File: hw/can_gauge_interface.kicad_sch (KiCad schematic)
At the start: 15 parts, among them J3 Power debug, J4 Power debug, J5 SPI debug, J6 I^{2}C debug, J7 CAN debug, U6 ATA6563-GAQW1

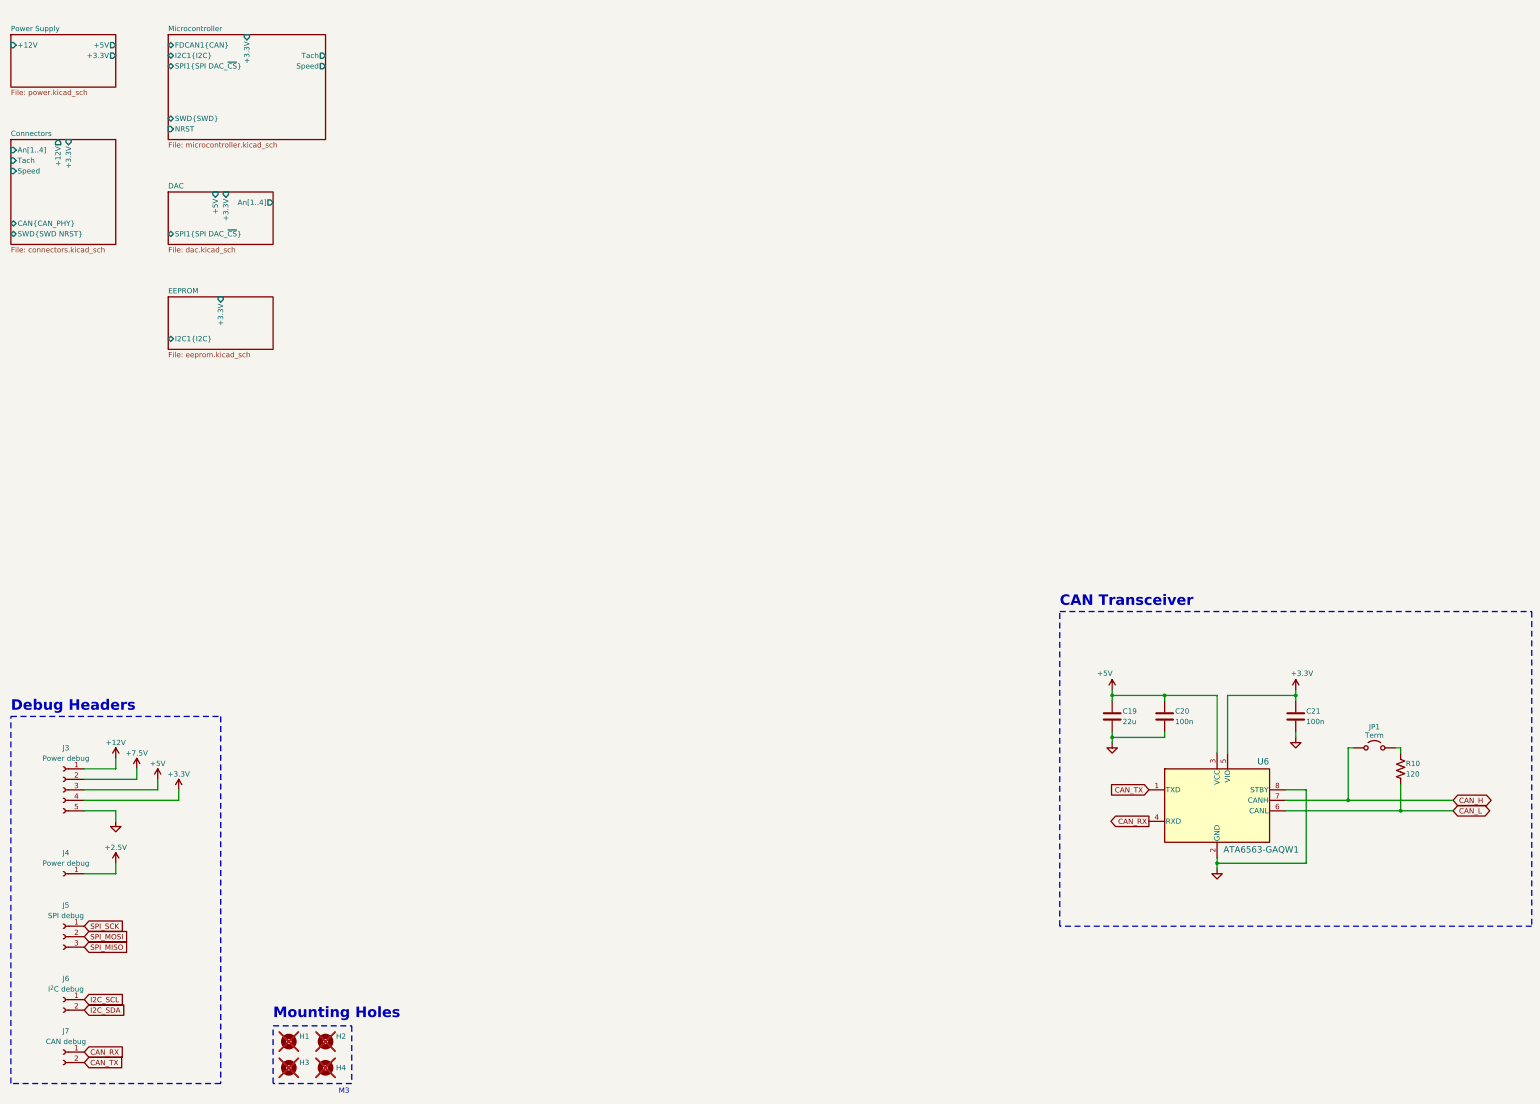
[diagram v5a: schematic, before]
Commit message: hw: can transceiver hierarchical sheet
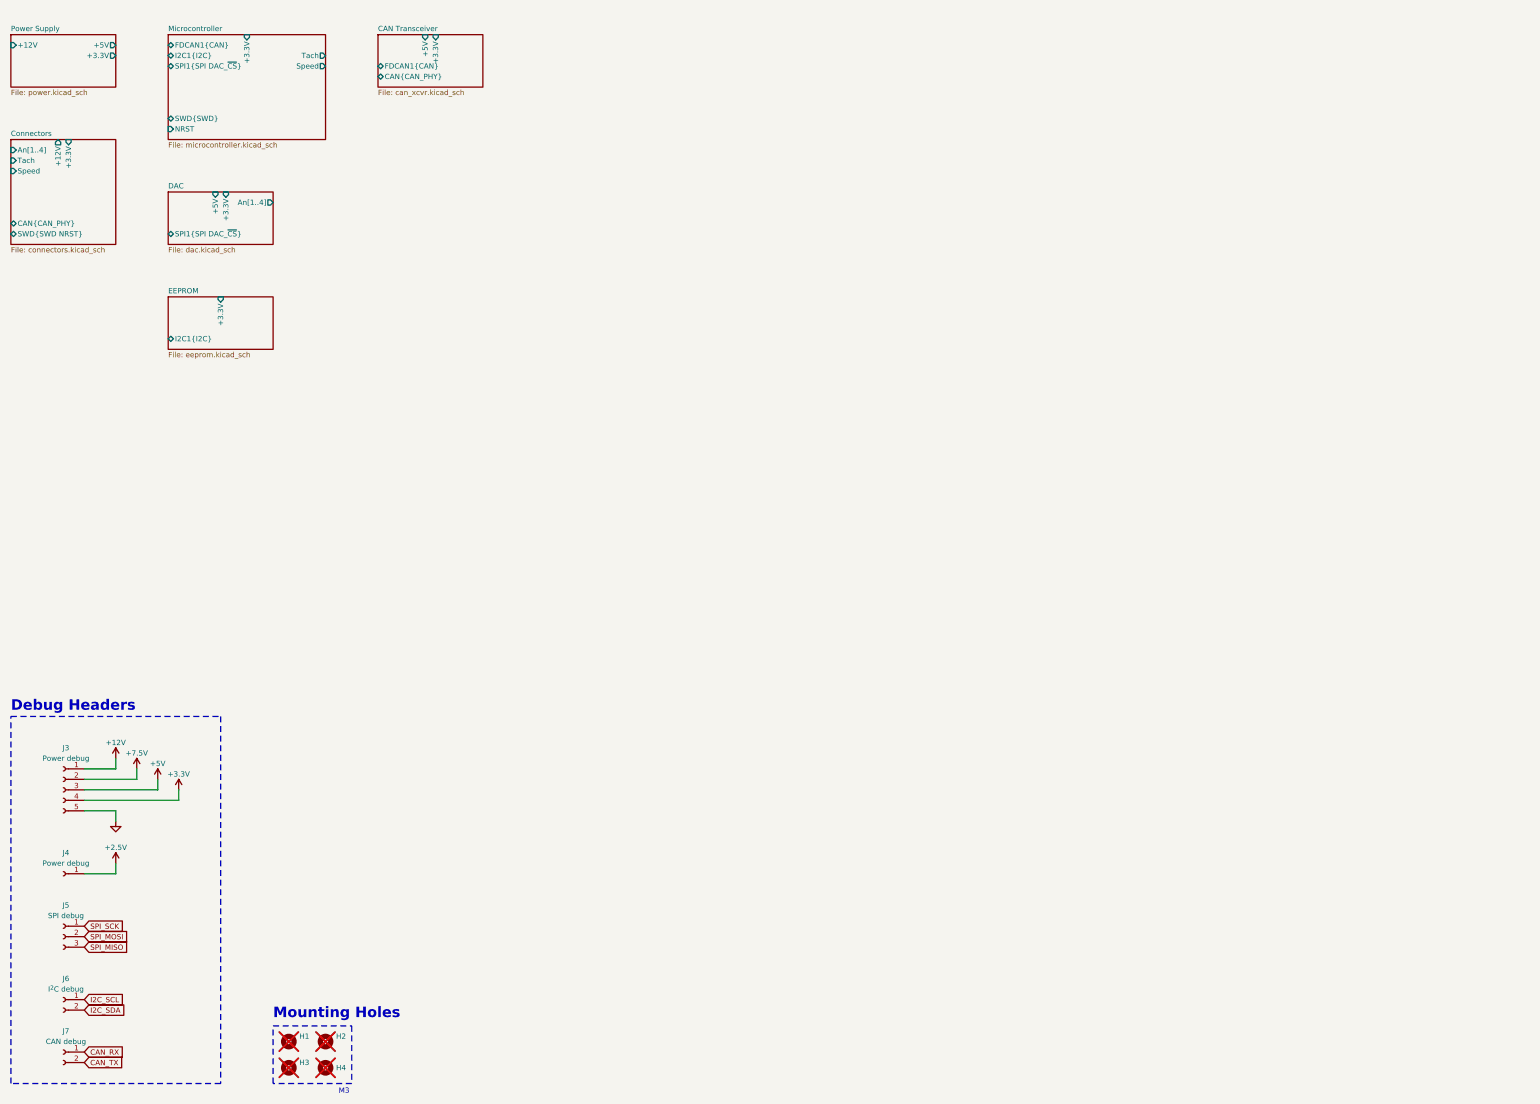
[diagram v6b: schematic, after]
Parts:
- removed C19: 22u, Capacitor_SMD:C_1206_3216Metric, symbol Device:C
- removed C20, C21: 100n, Capacitor_SMD:C_0402_1005Metric, symbol Device:C
- removed JP1: Term, TestPoint:TestPoint_2Pads_Pitch2.54mm_Drill0.8mm, symbol Jumper:Jumper_2_Open
- removed R10: 120, Resistor_SMD:R_0603_1608Metric, symbol Device:R_US
- removed U6: ATA6563-GAQW1, footprints:SOIC8_SN_MCH, symbol ATA6563-GAQW1:ATA6563-GAQW1
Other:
- added sheet CAN Transceiver (can_xcvr.kicad_sch)
- note removed: "CAN Transceiver"

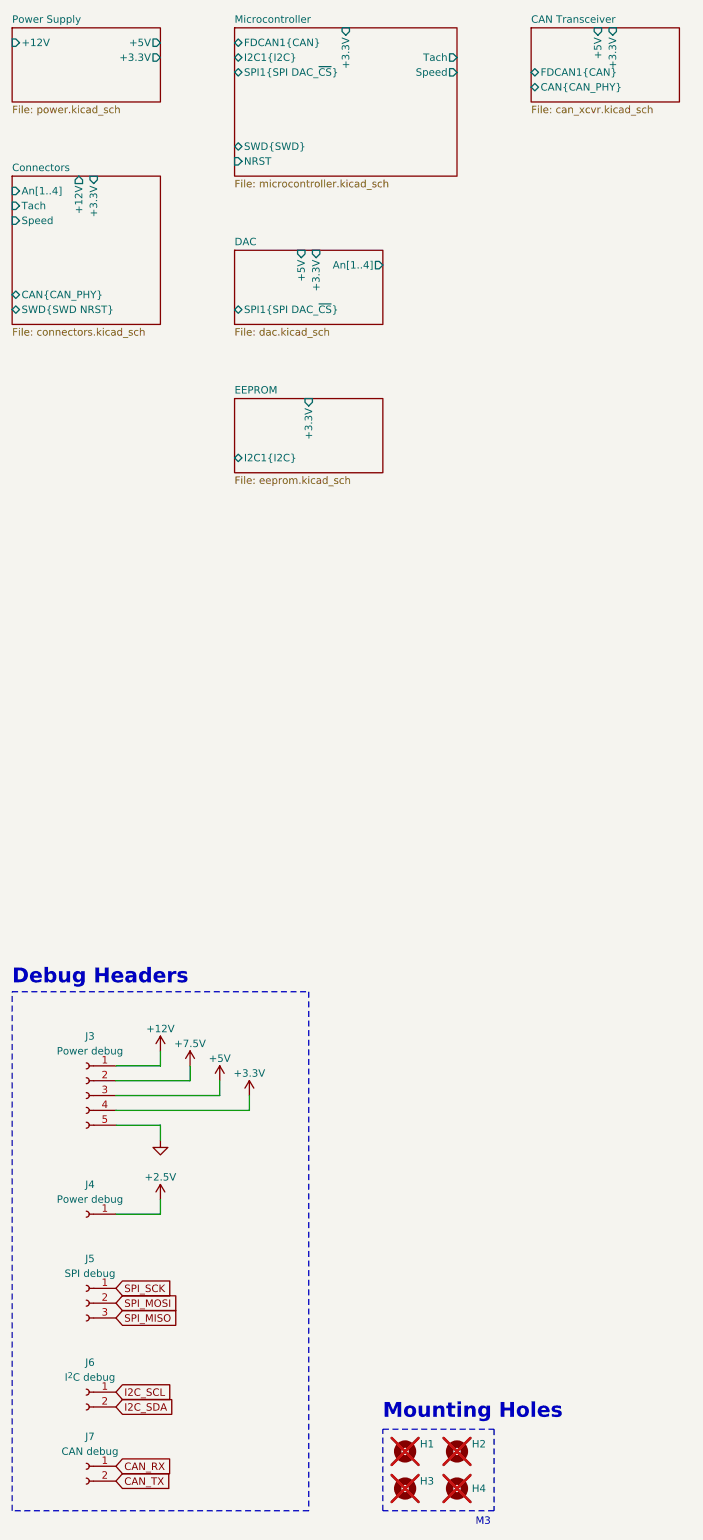
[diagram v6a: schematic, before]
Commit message: hw: headers hierarchical sheet
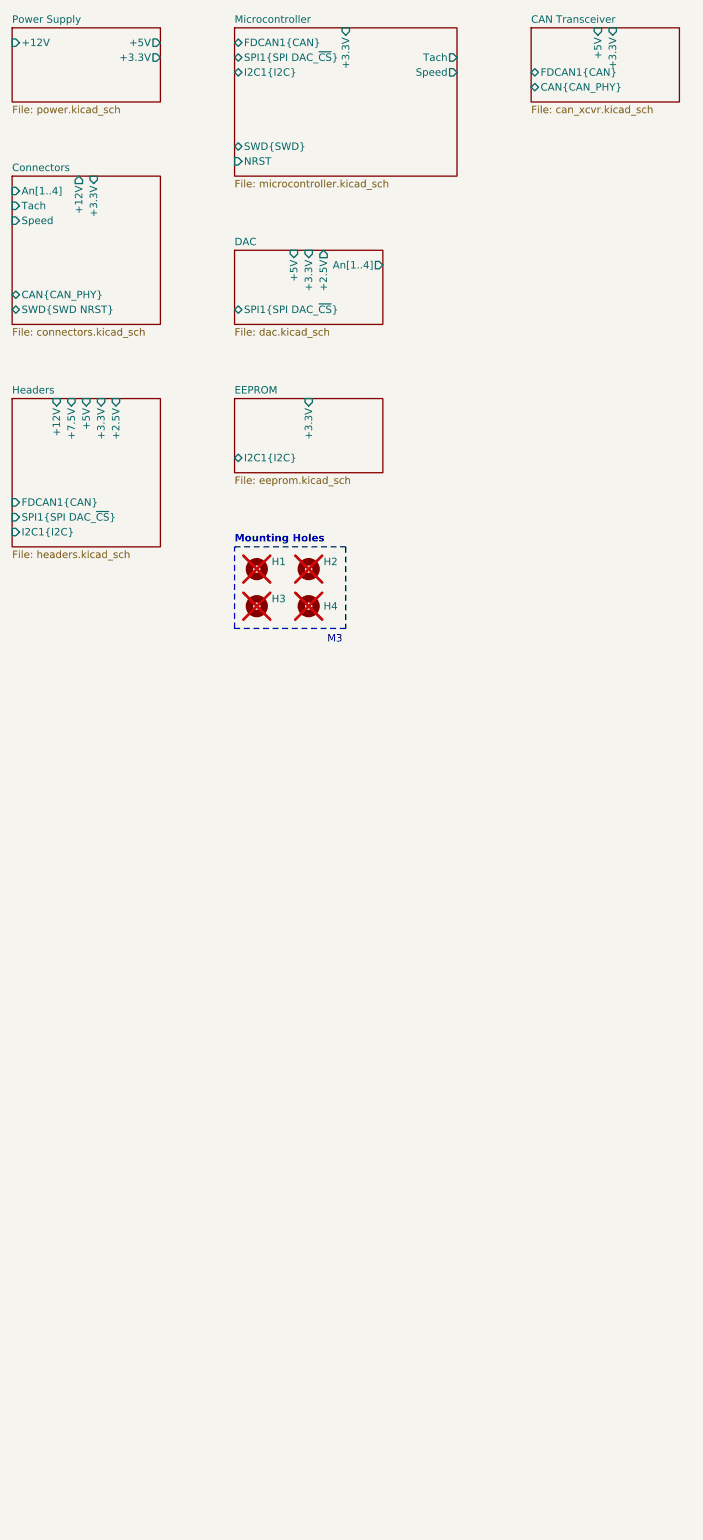
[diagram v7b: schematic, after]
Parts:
- removed J3: Power debug, Connector_PinSocket_2.54mm:PinSocket_1x05_P2.54mm_Vertical, symbol Connector:Conn_01x05_Socket
- removed J4: Power debug, Connector_PinSocket_2.54mm:PinSocket_1x01_P2.54mm_Vertical, symbol Connector:Conn_01x01_Socket
- removed J5: SPI debug, Connector_PinSocket_2.54mm:PinSocket_1x03_P2.54mm_Vertical, symbol Connector:Conn_01x03_Socket
- removed J6: I^{2}C debug, Connector_PinSocket_2.54mm:PinSocket_1x02_P2.54mm_Vertical, symbol Connector:Conn_01x02_Socket
- removed J7: CAN debug, Connector_PinSocket_2.54mm:PinSocket_1x02_P2.54mm_Vertical, symbol Connector:Conn_01x02_Socket
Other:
- added sheet Headers (headers.kicad_sch)
- sheet DAC ports: added +2.5V; removed none
- note removed: "Debug Headers"
- moved on the sheet: H1, H2, H3, H4

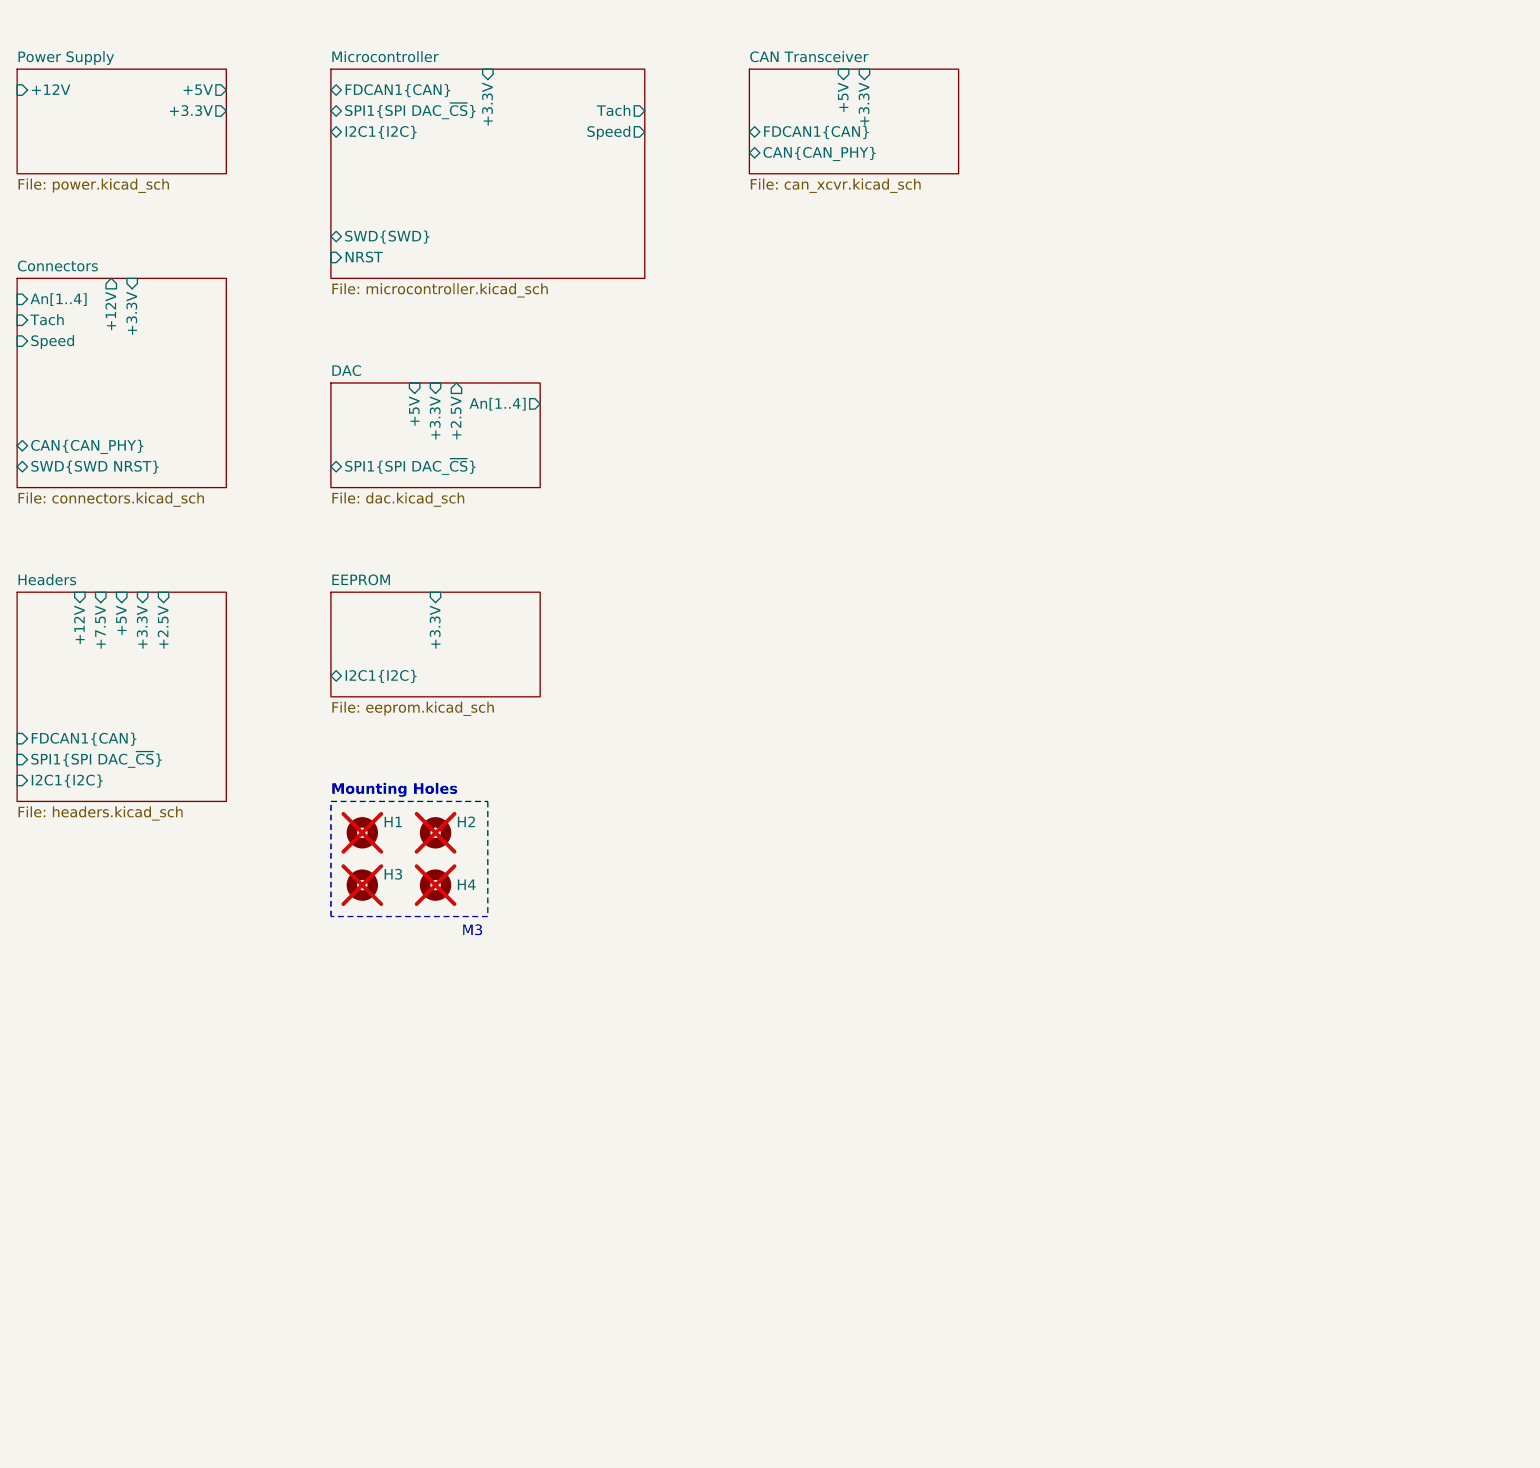
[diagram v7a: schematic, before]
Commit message: hw: top level schematic
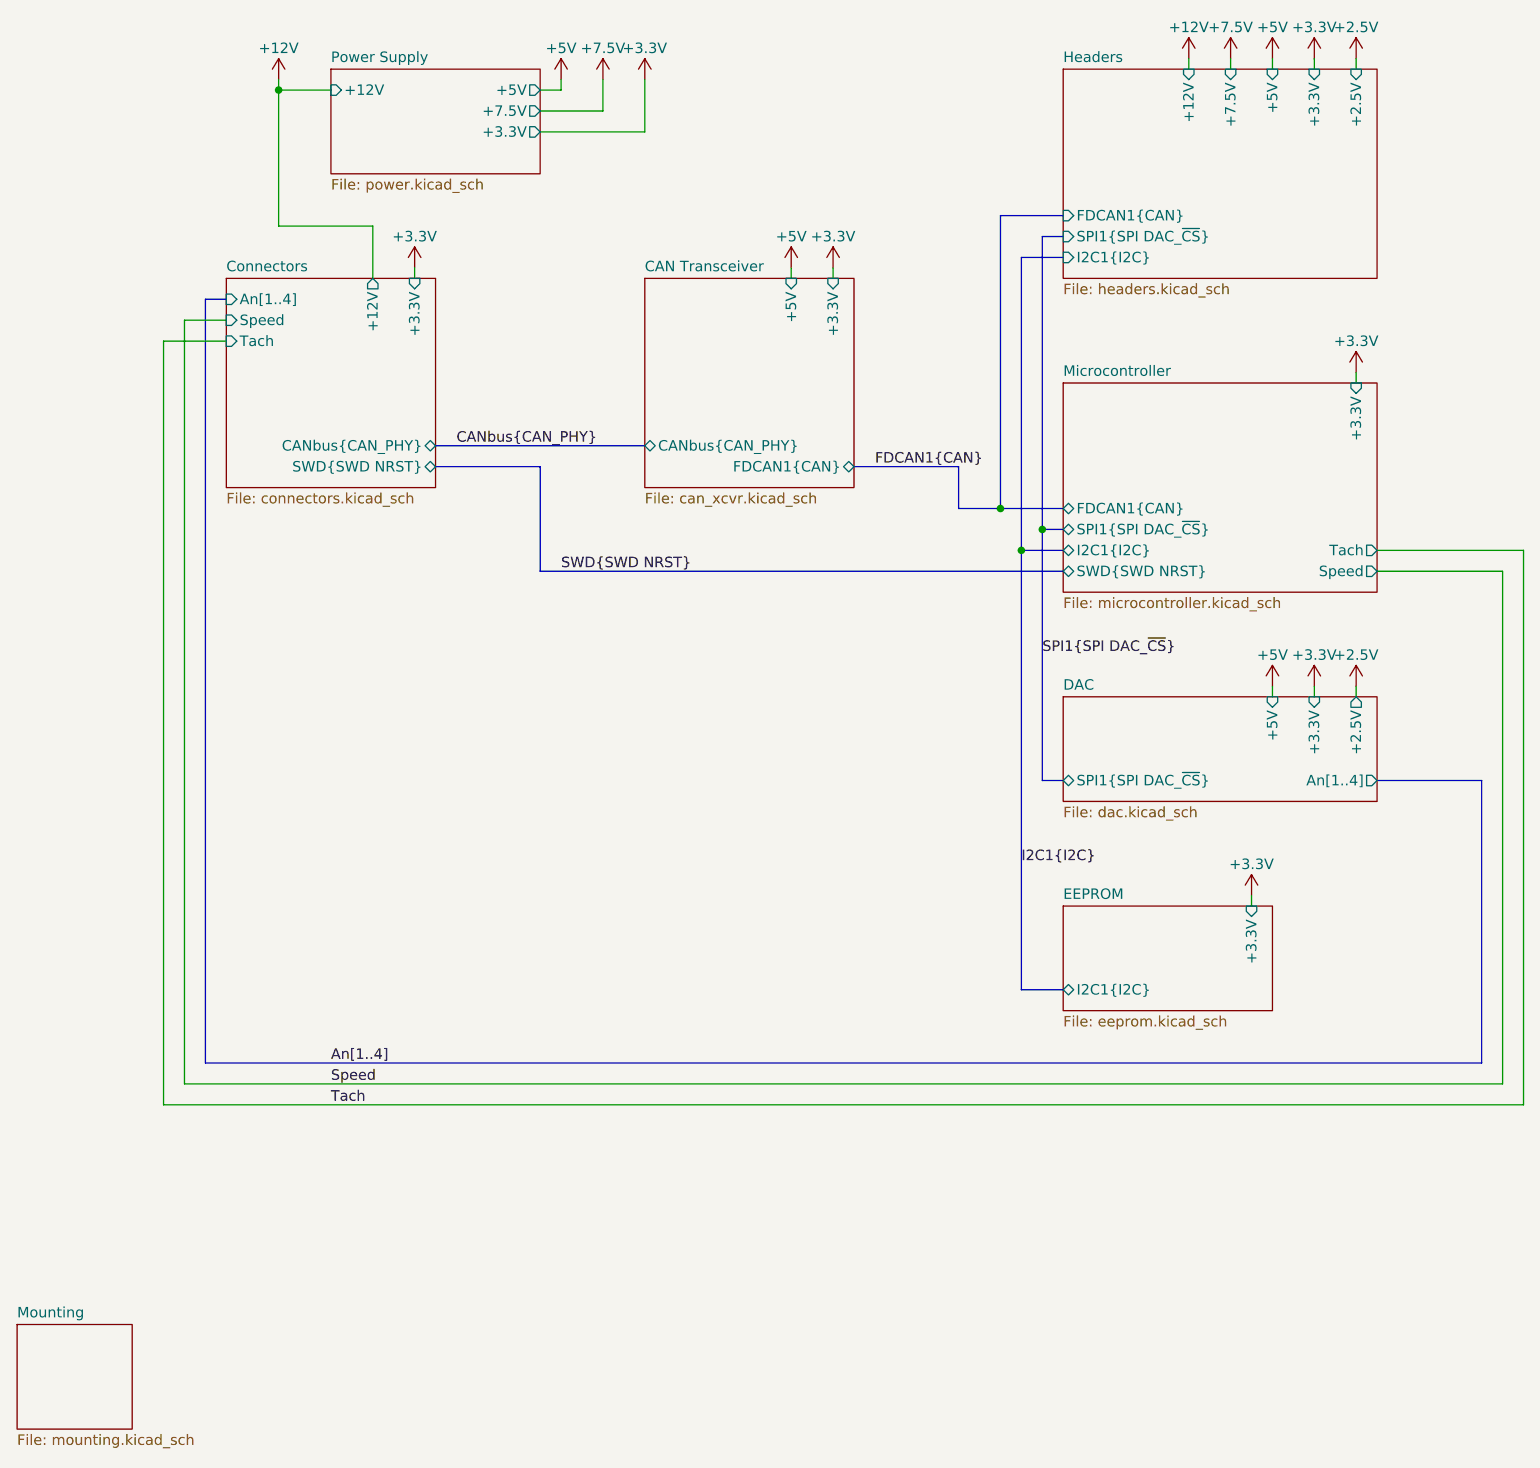
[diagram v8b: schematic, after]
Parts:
- removed H1, H2, H3, H4: MountingHole, MountingHole:MountingHole_3.2mm_M3_DIN965, symbol Mechanical:MountingHole
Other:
- added sheet Mounting (mounting.kicad_sch)
- sheet CAN Transceiver ports: added CANbus{CAN_PHY}; removed CAN{CAN_PHY}
- sheet Connectors ports: added CANbus{CAN_PHY}; removed CAN{CAN_PHY}
- sheet Microcontroller ports: added SWD{SWD NRST}; removed NRST, SWD{SWD}
- sheet Power Supply ports: added +7.5V; removed none
- note removed: "M3"
- note removed: "Mounting Holes"
